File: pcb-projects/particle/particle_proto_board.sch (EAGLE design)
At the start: 1 part, among them IC1 ATTINY20-SOIC-14S1

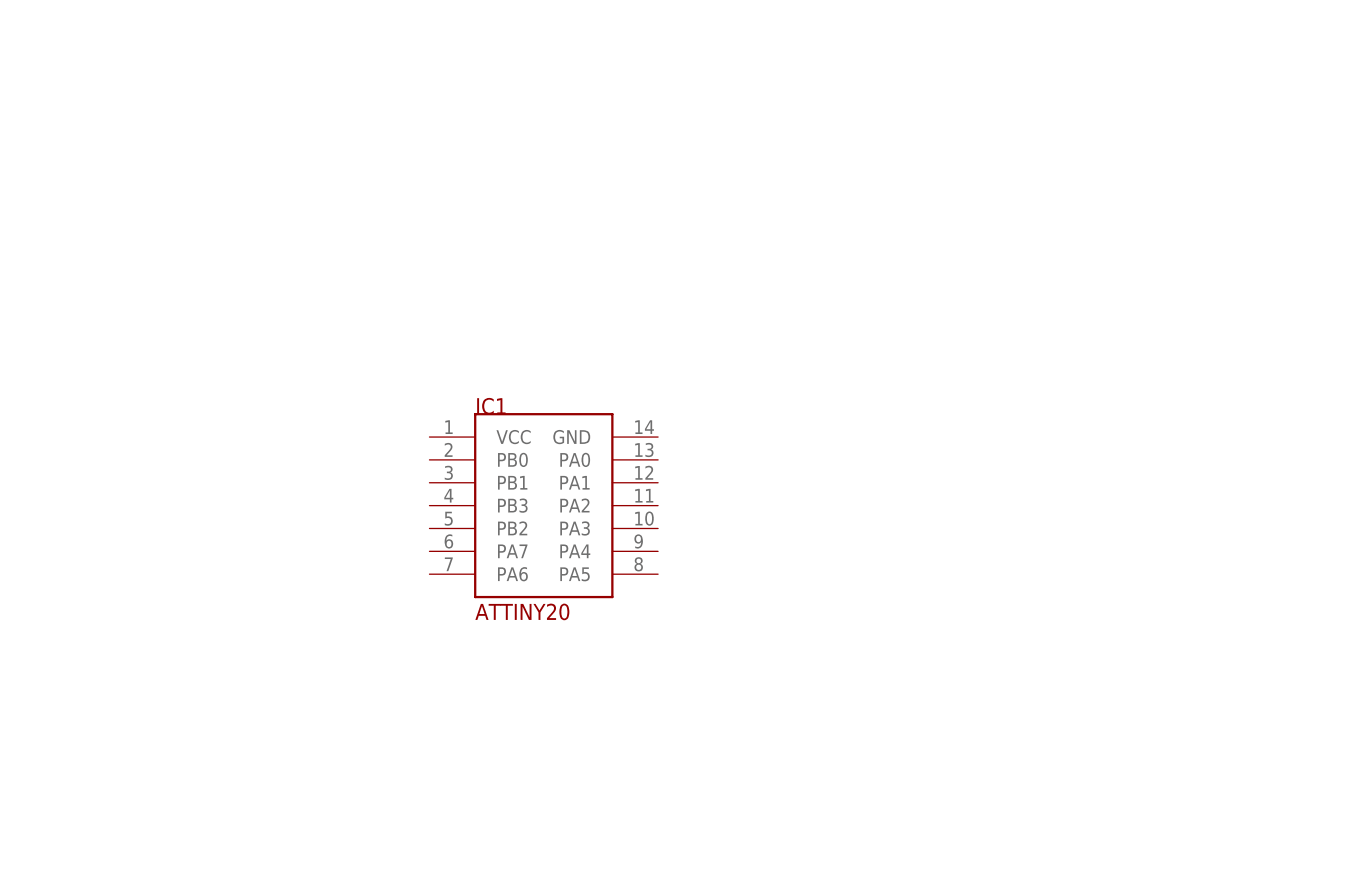
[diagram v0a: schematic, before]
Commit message: connected h-bridges to comm wires
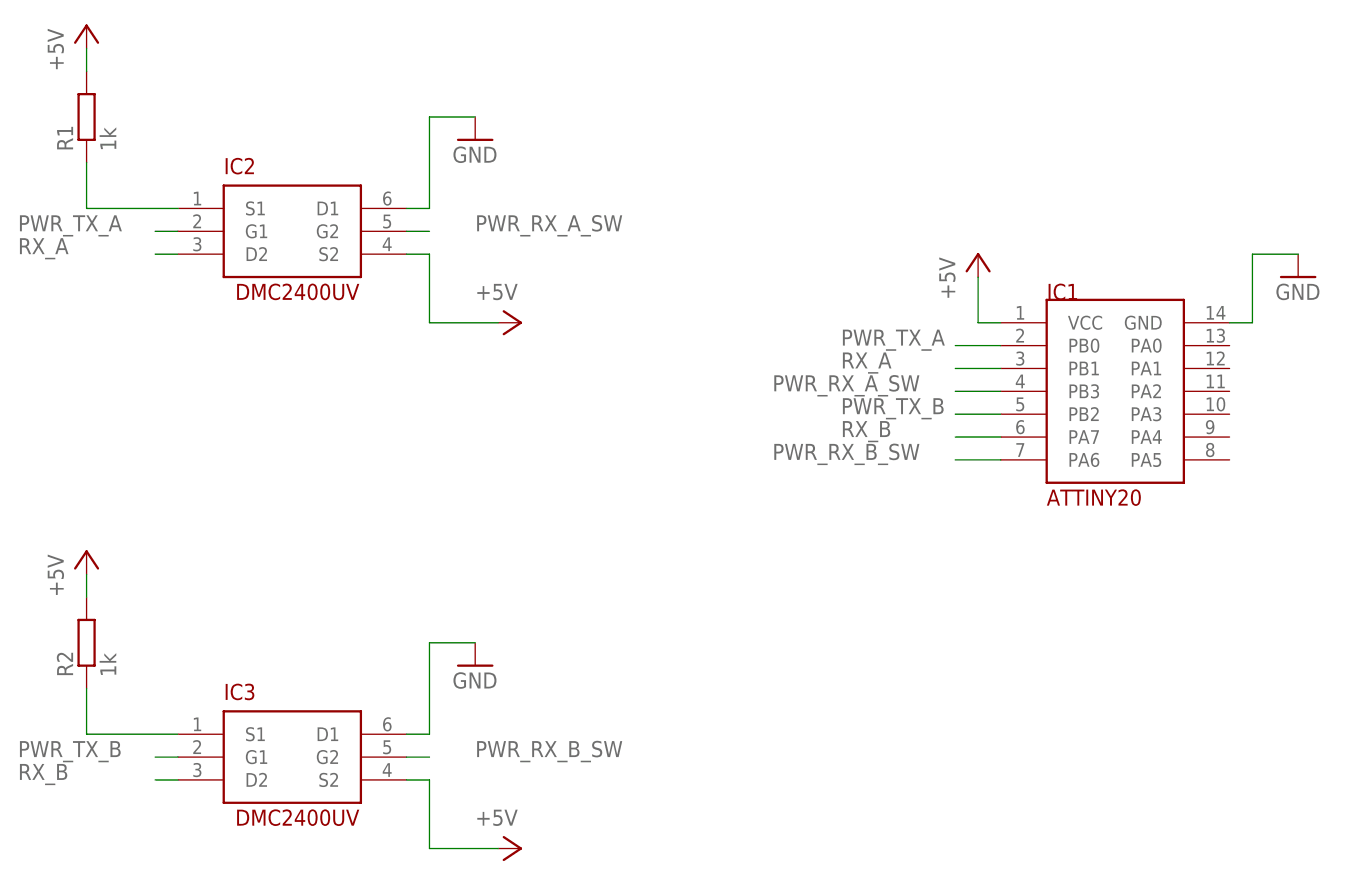
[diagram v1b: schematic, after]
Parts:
- added IC2, IC3: DMC2400UV-SOT563, dmc2400uv:DMC2400UV-SOT563
- added R1, R2: 1k, rcl:R-EU_R1206
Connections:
- new net +5V: IC1.VCC, IC2.S2, IC3.S2, R1.2, R2.2
- new net GND: IC1.GND, IC2.D1, IC3.D1
- new net PWR_RX_A_SW: IC1.PB3, IC2.G2
- new net PWR_RX_B_SW: IC1.PA6, IC3.G2
- new net PWR_TX_A: IC1.PB0, IC2.G1
- new net PWR_TX_A_A_A: IC2.S1, R1.1
- new net PWR_TX_A_A_A1: IC3.S1, R2.1
- new net PWR_TX_B: IC1.PB2, IC3.G1
- new net RX_A: IC1.PB1, IC2.D2
- new net RX_B: IC1.PA7, IC3.D2
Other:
- moved on the sheet: IC1
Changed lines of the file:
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@@
 <layer number="97" name="Info" color="7" fill="1" visible="yes" active="yes"/>
 <layer number="98" name="Guide" color="6" fill="1" visible="yes" active="yes"/>
+<layer number="99" name="SpiceOrder" color="5" fill="1" visible="yes" active="yes"/>
 </layers>
 <schematic xreflabel="%F%N/%S.%C%R" xrefpart="/%S.%C%R">
@@
 <parts>
 <part name="IC1" library="ic-attiny20" deviceset="ATTINY20-SOIC-14S1" device=""/>
+<part name="IC2" library="dmc2400uv" deviceset="DMC2400UV-SOT563" device=""/>
+<part name="P+2" library="supply1" deviceset="+5V" device=""/>
+<part name="GND1" library="supply1" deviceset="GND" device=""/>
+<part name="GND2" library="supply1" deviceset="GND" device=""/>
+<part name="P+1" library="supply1" deviceset="+5V" device=""/>
+<part name="P+3" library="supply1" deviceset="+5V" device=""/>
+<part name="IC3" library="dmc2400uv" deviceset="DMC2400UV-SOT563" device=""/>
+<part name="GND3" library="supply1" deviceset="GND" device=""/>
+<part name="P+4" library="supply1" deviceset="+5V" device=""/>
+<part name="P+5" library="supply1" deviceset="+5V" device=""/>
+<part name="R1" library="rcl" deviceset="R-EU_" device="R1206" value="1k"/>
+<part name="R2" library="rcl" deviceset="R-EU_" device="R1206" value="1k"/>
 </parts>
 <sheets>
@@
 </plain>
 <instances>
-<instance part="IC1" gate="G$1" x="27.94" y="71.12"/>
+<instance part="IC1" gate="G$1" x="91.44" y="83.82"/>
+<instance part="IC2" gate="G$1" x="0" y="101.6"/>
+<instance part="P+2" gate="1" x="76.2" y="99.06"/>
+<instance part="GND1" gate="1" x="111.76" y="96.52"/>
+<instance part="GND2" gate="1" x="20.32" y="111.76"/>
+<instance part="P+1" gate="1" x="-22.86" y="124.46"/>
+<instance part="P+3" gate="1" x="25.4" y="91.44" rot="R270"/>
+<instance part="IC3" gate="G$1" x="0" y="43.18"/>
+<instance part="GND3" gate="1" x="20.32" y="53.34"/>
+<instance part="P+4" gate="1" x="-22.86" y="66.04"/>
+<instance part="P+5" gate="1" x="25.4" y="33.02" rot="R270"/>
+<instance part="R1" gate="G$1" x="-22.86" y="114.3" rot="R90"/>
+<instance part="R2" gate="G$1" x="-22.86" y="55.88" rot="R90"/>
 </instances>
 <busses>
 </busses>
 <nets>
+<net name="+5V" class="0">
+<segment>
+<pinref part="IC1" gate="G$1" pin="VCC"/>
+<wire x1="78.74" y1="91.44" x2="76.2" y2="91.44" width="0.1524" layer="91"/>
+<wire x1="76.2" y1="91.44" x2="76.2" y2="96.52" width="0.1524" layer="91"/>
+<pinref part="P+2" gate="1" pin="+5V"/>
+</segment>
+<segment>
+<wire x1="-22.86" y1="119.38" x2="-22.86" y2="121.92" width="0.1524" layer="91"/>
+<pinref part="P+1" gate="1" pin="+5V"/>
+<pinref part="R1" gate="G$1" pin="2"/>
+</segment>
+<segment>
+<pinref part="IC2" gate="G$1" pin="S2"/>
+<wire x1="12.7" y1="99.06" x2="15.24" y2="99.06" width="0.1524" layer="91"/>
+<wire x1="15.24" y1="99.06" x2="15.24" y2="91.44" width="0.1524" layer="91"/>
+<pinref part="P+3" gate="1" pin="+5V"/>
+<wire x1="15.24" y1="91.44" x2="22.86" y2="91.44" width="0.1524" layer="91"/>
+</segment>
+<segment>
+<wire x1="-22.86" y1="60.96" x2="-22.86" y2="63.5" width="0.1524" layer="91"/>
+<pinref part="P+4" gate="1" pin="+5V"/>
+<pinref part="R2" gate="G$1" pin="2"/>
+</segment>
+<segment>
+<pinref part="IC3" gate="G$1" pin="S2"/>
+<wire x1="12.7" y1="40.64" x2="15.24" y2="40.64" width="0.1524" layer="91"/>
+<wire x1="15.24" y1="40.64" x2="15.24" y2="33.02" width="0.1524" layer="91"/>
+<pinref part="P+5" gate="1" pin="+5V"/>
+<wire x1="15.24" y1="33.02" x2="22.86" y2="33.02" width="0.1524" layer="91"/>
+</segment>
+</net>
+<net name="GND" class="0">
+<segment>
+<pinref part="IC1" gate="G$1" pin="GND"/>
+<wire x1="104.14" y1="91.44" x2="106.68" y2="91.44" width="0.1524" layer="91"/>
+<wire x1="106.68" y1="91.44" x2="106.68" y2="99.06" width="0.1524" layer="91"/>
+<pinref part="GND1" gate="1" pin="GND"/>
+<wire x1="106.68" y1="99.06" x2="111.76" y2="99.06" width="0.1524" layer="91"/>
+</segment>
+<segment>
+<pinref part="IC2" gate="G$1" pin="D1"/>
+<wire x1="12.7" y1="104.14" x2="15.24" y2="104.14" width="0.1524" layer="91"/>
+<wire x1="15.24" y1="104.14" x2="15.24" y2="114.3" width="0.1524" layer="91"/>
+<pinref part="GND2" gate="1" pin="GND"/>
+<wire x1="15.24" y1="114.3" x2="20.32" y2="114.3" width="0.1524" layer="91"/>
+</segment>
+<segment>
+<pinref part="IC3" gate="G$1" pin="D1"/>
+<wire x1="12.7" y1="45.72" x2="15.24" y2="45.72" width="0.1524" layer="91"/>
+<wire x1="15.24" y1="45.72" x2="15.24" y2="55.88" width="0.1524" layer="91"/>
+<pinref part="GND3" gate="1" pin="GND"/>
+<wire x1="15.24" y1="55.88" x2="20.32" y2="55.88" width="0.1524" layer="91"/>
+</segment>
+</net>
+<net name="PWR_TX_A" class="0">
+<segment>
+<pinref part="IC1" gate="G$1" pin="PB0"/>
+<wire x1="78.74" y1="88.9" x2="73.66" y2="88.9" width="0.1524" layer="91"/>
+<label x="60.96" y="88.9" size="1.778" layer="95"/>
+</segment>
+<segment>
+<pinref part="IC2" gate="G$1" pin="G1"/>
+<wire x1="-12.7" y1="101.6" x2="-15.24" y2="101.6" width="0.1524" layer="91"/>
+<label x="-30.48" y="101.6" size="1.778" layer="95"/>
+</segment>
+</net>
+<net name="PWR_TX_B" class="0">
+<segment>
+<pinref part="IC1" gate="G$1" pin="PB2"/>
+<wire x1="78.74" y1="81.28" x2="73.66" y2="81.28" width="0.1524" layer="91"/>
+<label x="60.96" y="81.28" size="1.778" layer="95"/>
+</segment>
+<segment>
+<pinref part="IC3" gate="G$1" pin="G1"/>
+<wire x1="-12.7" y1="43.18" x2="-15.24" y2="43.18" width="0.1524" layer="91"/>
+<label x="-30.48" y="43.18" size="1.778" layer="95"/>
+</segment>
+</net>
+<net name="RX_A" class="0">
+<segment>
+<pinref part="IC1" gate="G$1" pin="PB1"/>
+<wire x1="78.74" y1="86.36" x2="73.66" y2="86.36" width="0.1524" layer="91"/>
+<label x="60.96" y="86.36" size="1.778" layer="95"/>
+</segment>
+<segment>
+<pinref part="IC2" gate="G$1" pin="D2"/>
+<wire x1="-12.7" y1="99.06" x2="-15.24" y2="99.06" width="0.1524" layer="91"/>
+<label x="-30.48" y="99.06" size="1.778" layer="95"/>
+</segment>
+</net>
+<net name="PWR_RX_A_SW" class="0">
+<segment>
+<pinref part="IC1" gate="G$1" pin="PB3"/>
+<wire x1="78.74" y1="83.82" x2="73.66" y2="83.82" width="0.1524" layer="91"/>
+<label x="53.34" y="83.82" size="1.778" layer="95"/>
+</segment>
+<segment>
+<pinref part="IC2" gate="G$1" pin="G2"/>
+<wire x1="12.7" y1="101.6" x2="15.24" y2="101.6" width="0.1524" layer="91"/>
+<label x="20.32" y="101.6" size="1.778" layer="95"/>
+</segment>
+</net>
+<net name="RX_B" class="0">
+<segment>
+<pinref part="IC1" gate="G$1" pin="PA7"/>
+<wire x1="78.74" y1="78.74" x2="73.66" y2="78.74" width="0.1524" layer="91"/>
+<label x="60.96" y="78.74" size="1.778" layer="95"/>
+</segment>
+<segment>
+<pinref part="IC3" gate="G$1" pin="D2"/>
+<wire x1="-12.7" y1="40.64" x2="-15.24" y2="40.64" width="0.1524" layer="91"/>
+<label x="-30.48" y="40.64" size="1.778" layer="95"/>
+</segment>
+</net>
+<net name="PWR_RX_B_SW" class="0">
+<segment>
+<pinref part="IC1" gate="G$1" pin="PA6"/>
+<wire x1="78.74" y1="76.2" x2="73.66" y2="76.2" width="0.1524" layer="91"/>
+<label x="53.34" y="76.2" size="1.778" layer="95"/>
+</segment>
+<segment>
+<pinref part="IC3" gate="G$1" pin="G2"/>
+<wire x1="12.7" y1="43.18" x2="15.24" y2="43.18" width="0.1524" layer="91"/>
+<label x="20.32" y="43.18" size="1.778" layer="95"/>
+</segment>
+</net>
+<net name="PWR_TX_A_A_A" class="0">
+<segment>
+<pinref part="IC2" gate="G$1" pin="S1"/>
+<wire x1="-12.7" y1="104.14" x2="-22.86" y2="104.14" width="0.1524" layer="91"/>
+<wire x1="-22.86" y1="104.14" x2="-22.86" y2="109.22" width="0.1524" layer="91"/>
+<pinref part="R1" gate="G$1" pin="1"/>
+</segment>
+</net>
+<net name="PWR_TX_A_A_A1" class="0">
+<segment>
+<pinref part="IC3" gate="G$1" pin="S1"/>
+<wire x1="-12.7" y1="45.72" x2="-22.86" y2="45.72" width="0.1524" layer="91"/>
+<wire x1="-22.86" y1="45.72" x2="-22.86" y2="50.8" width="0.1524" layer="91"/>
+<pinref part="R2" gate="G$1" pin="1"/>
+</segment>
+</net>
 </nets>
 </sheet>
